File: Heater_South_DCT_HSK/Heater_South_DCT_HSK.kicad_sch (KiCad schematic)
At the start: 3 parts, among them J1 South_Heater_1, J2 South_Heater_2, J3 Internal_Heater_DCT_HSK_Box

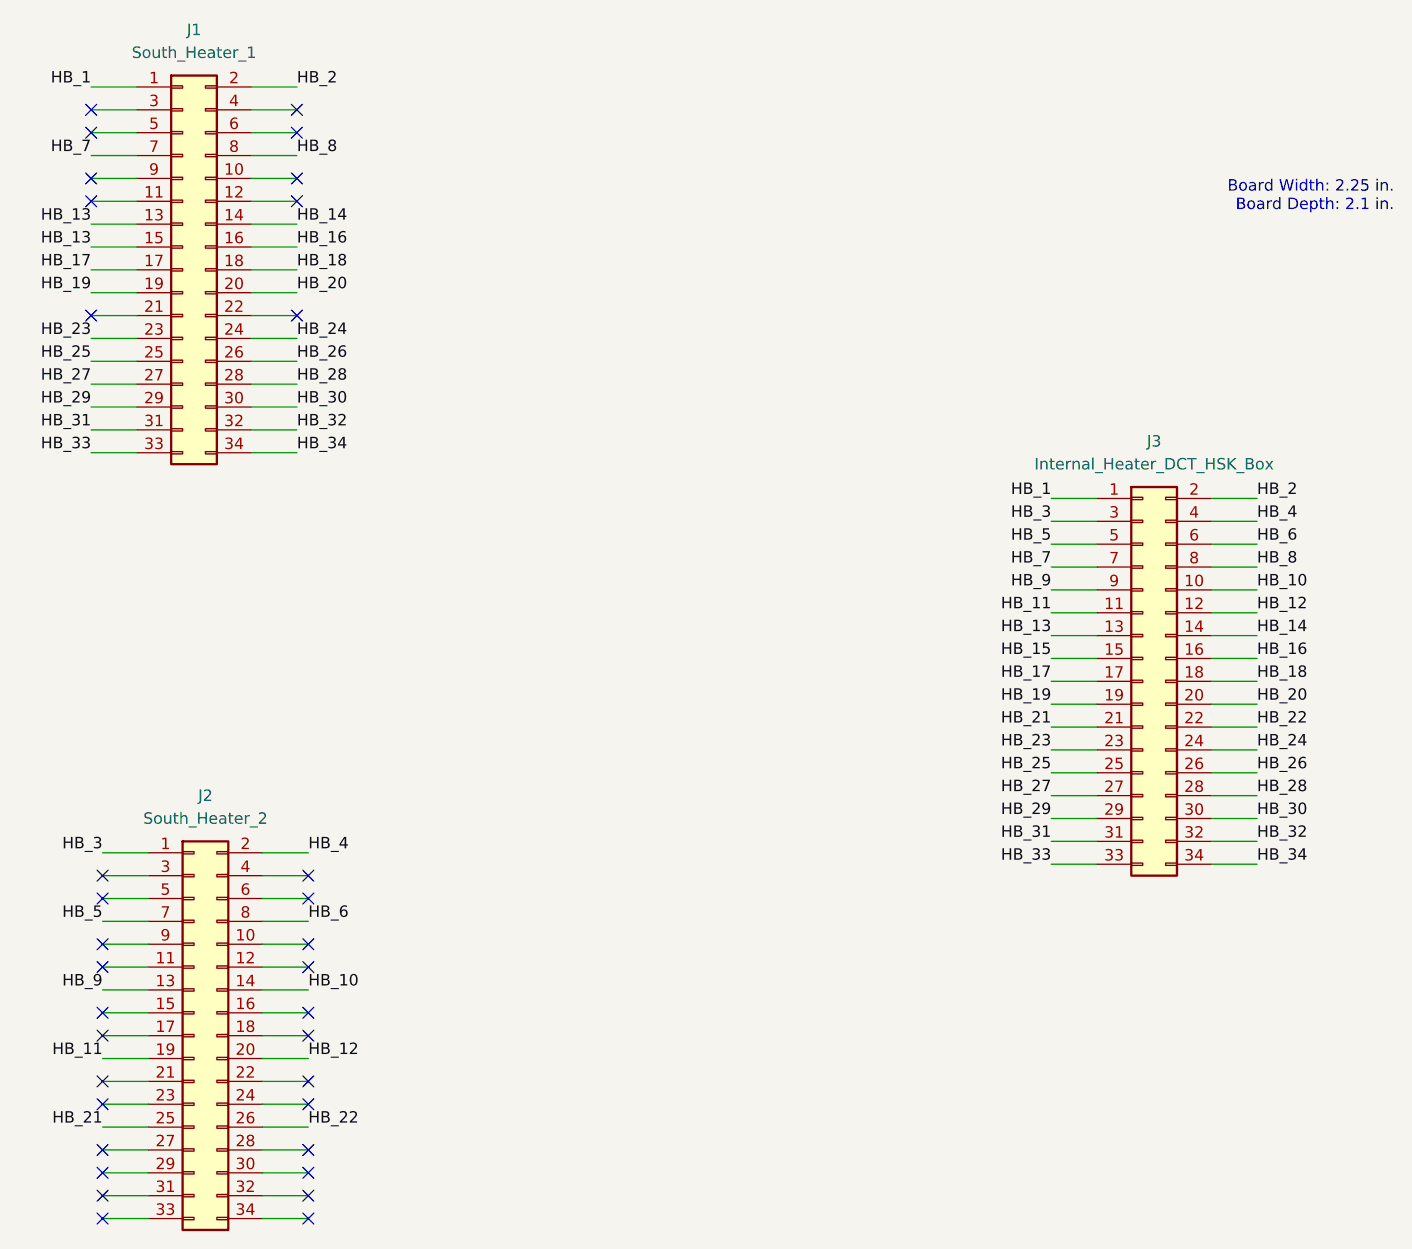
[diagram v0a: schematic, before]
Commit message: Updated Heater and Temp PCBs to board size 2.5in x 2.1in. Updated traces and silkscreens
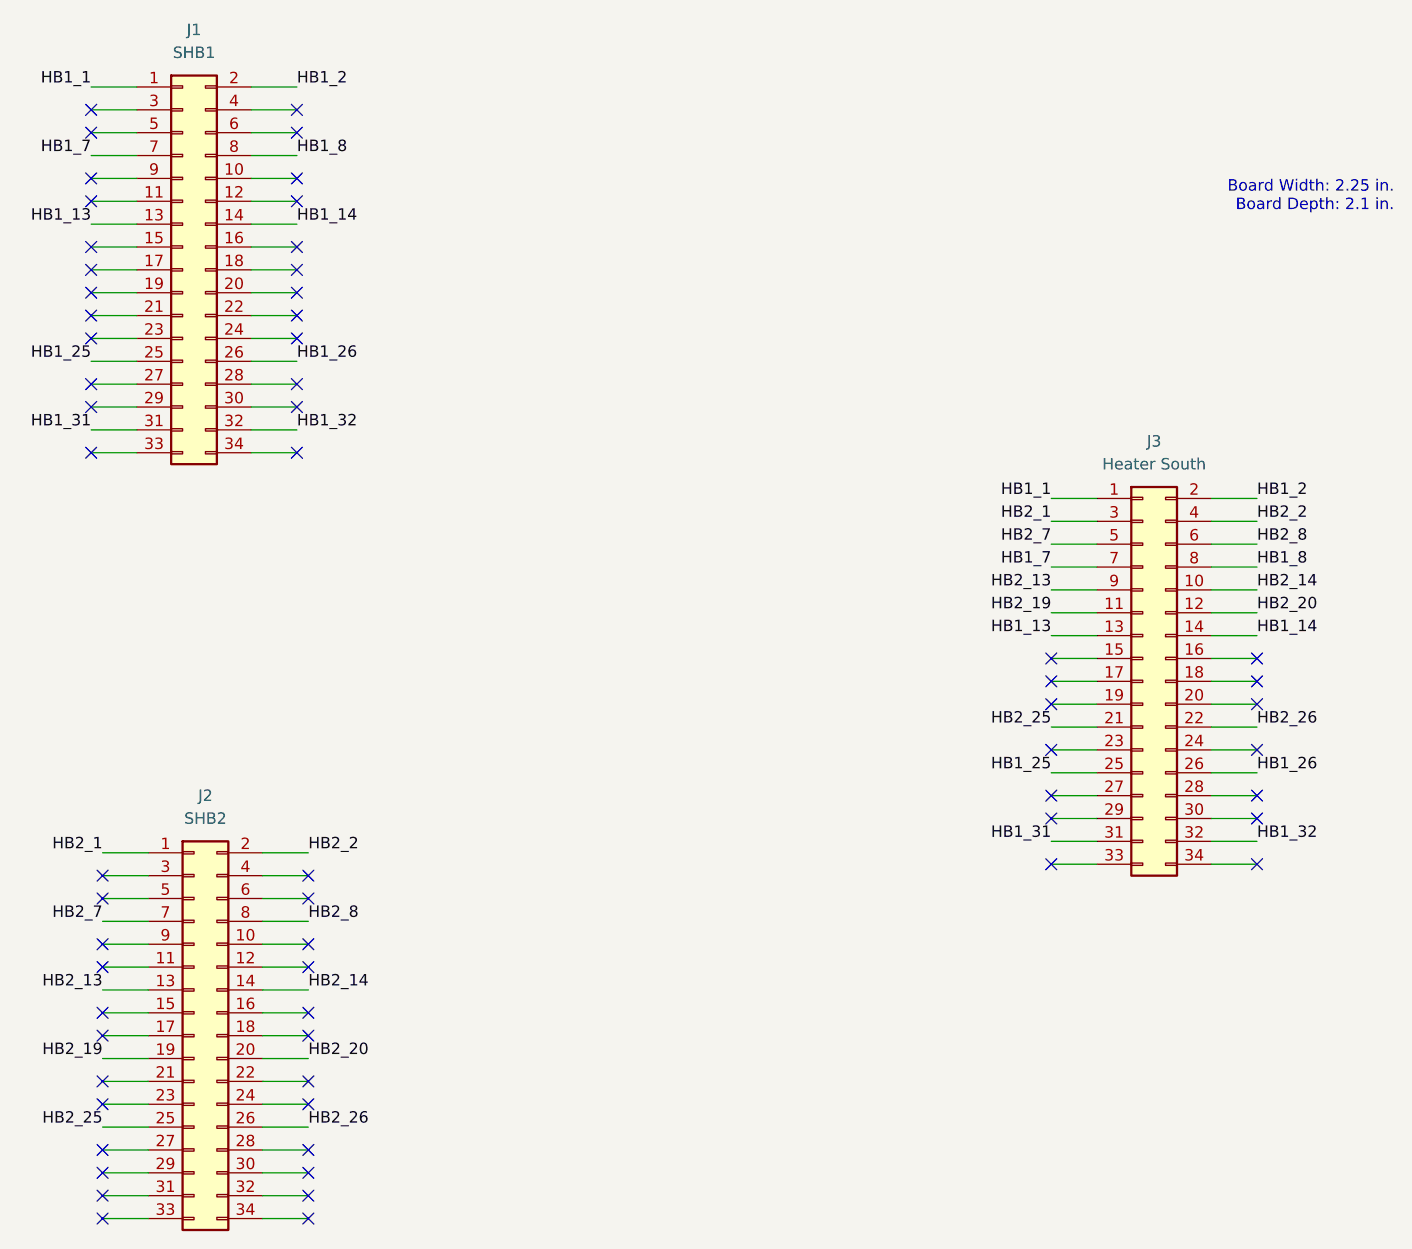
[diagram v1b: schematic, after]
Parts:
- J1: value South_Heater_1 -> SHB1
- J2: value South_Heater_2 -> SHB2
- J3: value Internal_Heater_DCT_HSK_Box -> Heater South
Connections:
- net HB_1 renamed HB1_1
- net HB_10 renamed HB2_14
- net HB_11 renamed HB2_19
- net HB_12 renamed HB2_20
- net HB_13 renamed HB1_13
- net HB1_13: no longer J1.15 (Pin_15)
- net HB_14 renamed HB1_14
- net HB_15: no longer names the net of J3.15 (Pin_15)
- net HB_16: no longer names the net of J3.16 (Pin_16)
- net HB_16: no longer J1.16 (Pin_16)
- net HB_17: no longer names the net of J3.17 (Pin_17)
- net HB_17: no longer J1.17 (Pin_17)
- net HB_18: no longer names the net of J3.18 (Pin_18)
- net HB_18: no longer J1.18 (Pin_18)
- net HB_19: no longer names the net of J3.19 (Pin_19)
- net HB_19: no longer J1.19 (Pin_19)
- net HB_2 renamed HB1_2
- net HB_20: no longer names the net of J3.20 (Pin_20)
- net HB_20: no longer J1.20 (Pin_20)
- net HB_21 renamed HB2_25
- net HB_22 renamed HB2_26
- net HB_23: no longer names the net of J3.23 (Pin_23)
- net HB_23: no longer J1.23 (Pin_23)
- net HB_24: no longer names the net of J3.24 (Pin_24)
- net HB_24: no longer J1.24 (Pin_24)
- net HB_25 renamed HB1_25
- net HB_26 renamed HB1_26
- net HB_27: no longer names the net of J3.27 (Pin_27)
- net HB_27: no longer J1.27 (Pin_27)
- net HB_28: no longer names the net of J3.28 (Pin_28)
- net HB_28: no longer J1.28 (Pin_28)
- net HB_29: no longer names the net of J3.29 (Pin_29)
- net HB_29: no longer J1.29 (Pin_29)
- net HB_3 renamed HB2_1
- net HB_30: no longer names the net of J3.30 (Pin_30)
- net HB_30: no longer J1.30 (Pin_30)
- net HB_31 renamed HB1_31
- net HB_32 renamed HB1_32
- net HB_33: no longer names the net of J3.33 (Pin_33)
- net HB_33: no longer J1.33 (Pin_33)
- net HB_34: no longer names the net of J3.34 (Pin_34)
- net HB_34: no longer J1.34 (Pin_34)
- net HB_4 renamed HB2_2
- net HB_5 renamed HB2_7
- net HB_6 renamed HB2_8
- net HB_7 renamed HB1_7
- net HB_8 renamed HB1_8
- net HB_9 renamed HB2_13
- no-connect marks 34 -> 62
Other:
- title: Heater Pass Through South -> Heater Pass Through North
